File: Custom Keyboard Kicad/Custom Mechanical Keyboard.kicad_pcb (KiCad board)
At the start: 2 copper layers, 327 x 114.5 mm, 326 parts, among them J3 Conn_01x05, J4 Conn_01x06, J5 Conn_01x07, J6 Conn_01x20_Socket, J7 Conn_01x20_Socket, SW1 SW_SPST, SW10 SW_SPST, SW11 SW_SPST, SW12 SW_SPST, SW13 SW_SPST, SW14 SW_SPST, SW15 SW_SPST, SW16 SW_SPST, SW17 SW_SPST, SW18 SW_SPST, SW19 SW_SPST, SW2 SW_SPST, SW20 SW_SPST, SW21 SW_SPST, SW22 SW_SPST, SW23 SW_SPST, SW24 SW_SPST, SW25 SW_SPST, SW26 SW_SPST, SW27 SW_SPST, SW28 SW_SPST, SW29 SW_SPST, SW3 SW_SPST, SW30 SW_SPST, SW31 SW_SPST, SW32 SW_SPST, SW33 SW_SPST, SW34 SW_SPST, SW35 SW_SPST, SW36 SW_SPST, SW37 SW_SPST, SW38 SW_SPST, SW39 SW_SPST, SW4 SW_SPST, SW40 SW_SPST, SW41 SW_SPST, SW42 SW_SPST, SW43 SW_SPST, SW44 SW_SPST, SW45 SW_SPST, SW46 SW_SPST, SW47 SW_SPST, SW48 SW_SPST, SW49 SW_SPST, SW5 SW_SPST, SW50 SW_SPST, SW51 SW_SPST, SW52 SW_SPST, SW53 SW_SPST, SW54 SW_SPST, SW55 SW_SPST, SW56 SW_SPST, SW57 SW_SPST, SW58 SW_SPST, SW59 SW_SPST, SW6 SW_SPST, SW60 SW_SPST, SW61 SW_SPST, SW62 SW_SPST, SW63 SW_SPST, SW64 SW_SPST, SW65 SW_SPST, SW66 SW_SPST, SW67 SW_SPST, SW68 SW_SPST, SW69 SW_SPST, SW7 SW_SPST, SW70 SW_SPST, SW71 SW_SPST, SW72 SW_SPST, SW73 SW_SPST, SW74 SW_SPST, SW75 SW_SPST, SW76 SW_SPST, SW77 SW_SPST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

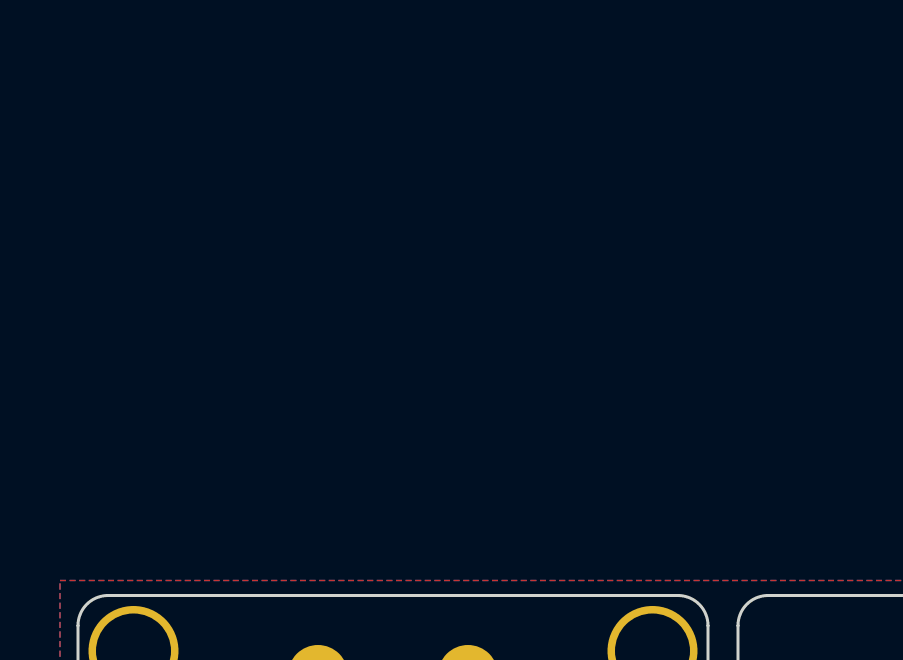
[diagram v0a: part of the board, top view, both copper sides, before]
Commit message: Feat: Added USB PCB, edited PCM Master Lib sunken usb-c port - changed pcb edge line to drawing to allow for edge cut line connection
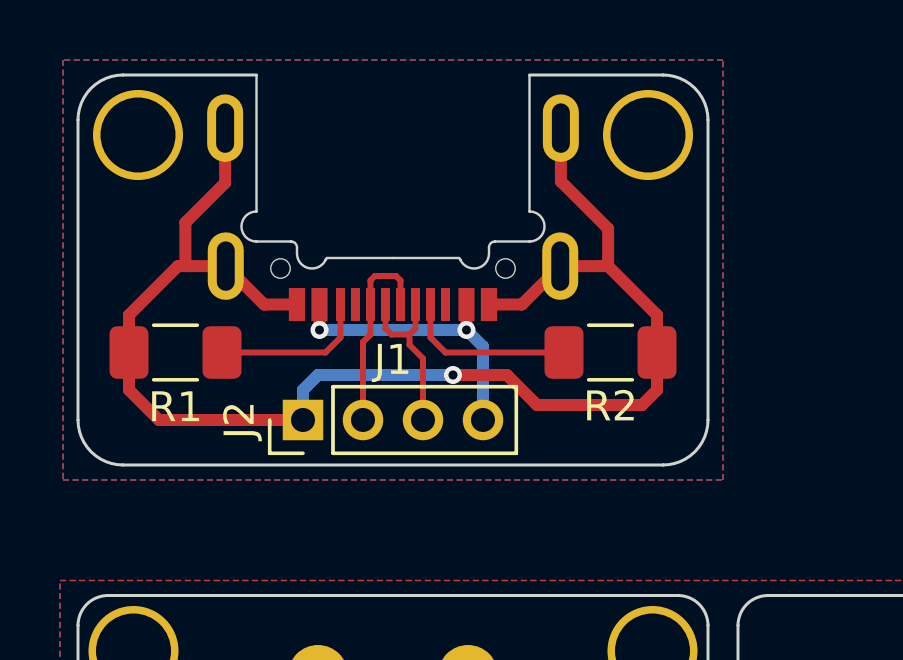
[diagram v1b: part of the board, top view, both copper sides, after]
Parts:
- added ?: , , F.Cu at (46.5, 32.1)
- added ?: , , F.Cu at (63.5, 32.1)
- added J1: USB_C_Receptacle_USB2.0_16P, PCM_marbastlib-various:USB_C_Receptacle_HRO_TYPE-C-31-M-14_(polygon_edge), F.Cu at (55.0, 36.6)
- added J2: Conn_01x04, Connector_PinHeader_2.00mm:PinHeader_1x04_P2.00mm_Vertical, F.Cu at (52.0, 41.6)
- added R1: 5.1k, Resistor_SMD:R_1206_3216Metric_Pad1.30x1.75mm_HandSolder, F.Cu at (47.8, 39.4)
- added R2: 5.1k, Resistor_SMD:R_1206_3216Metric_Pad1.30x1.75mm_HandSolder, F.Cu at (62.3, 39.4)
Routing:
- net USB_GND: track 0.00 -> 48.9 mm, vias 0 -> 1
- net /VBUS: track 0.00 -> 9.83 mm, vias 0 -> 2
- net /DP: track 0.00 -> 6.68 mm
- net /DM: track 0.00 -> 5.80 mm
- net Net-(J1-CC1): track 0.00 -> 5.61 mm
- net Net-(J1-CC2): track 0.00 -> 5.11 mm
- added copper zone on B.Cu, net USB_GND
- added copper zone on F.Cu, net USB_GND
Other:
- board size 327 x 114.5 mm -> 327 x 131.8 mm
